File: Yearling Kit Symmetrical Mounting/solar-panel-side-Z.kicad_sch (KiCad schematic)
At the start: 45 parts, among them J1 CON-5040500591, J2 Screw_Terminal_01x02, J3 Screw_Terminal_01x02, J4 Conn_01x01, J5 Conn_01x01, J6 Conn_01x01, J7 Conn_01x01, U1 VEML7700, U2 DRV2605LDGS, U3 MCP9808_DFN, U4 AD8495, U5 ADS1015IDGS, U6 TLVH431 DBZ SOT-23

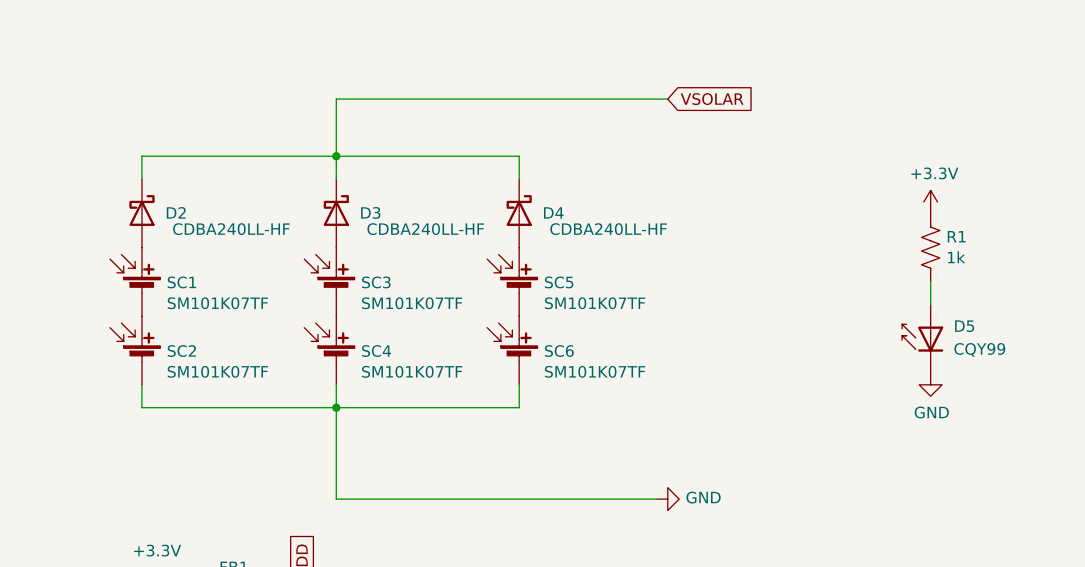
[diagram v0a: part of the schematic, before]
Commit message: -Z Face Mounting Changed
Holes are now symmetrical.
Typos in Silkscreen have been corrected.
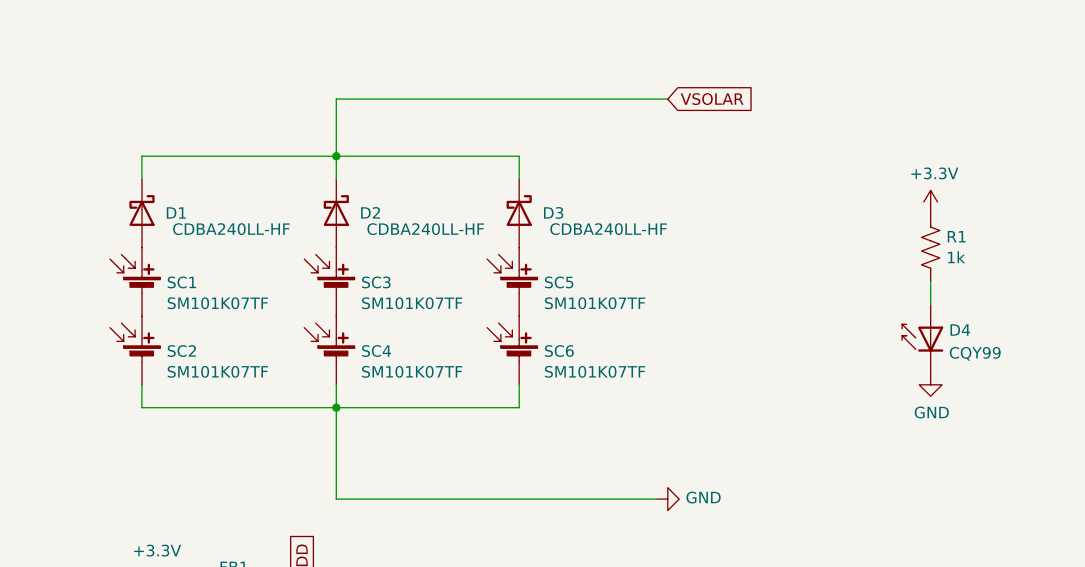
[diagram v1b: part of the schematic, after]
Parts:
- renumbered D2 to D1, D3 to D2, D4 to D3, D5 to D4
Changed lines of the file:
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@@
   (symbol (lib_id "Device:D_Schottky") (at 176.53 95.25 270) (unit 1)
     (in_bom yes) (on_board yes)
-    (property "Reference" "D2" (id 0) (at 180.34 95.25 90))
+    (property "Reference" "D1" (id 0) (at 180.34 95.25 90))
     (property "Value" "CDBA240LL-HF" (id 1) (at 193.04 97.79 90)
       (effects (font (size 1.27 1.27)) (justify right bottom))
@@
   (symbol (lib_id "Device:D_Schottky") (at 198.12 95.25 270) (unit 1)
     (in_bom yes) (on_board yes)
-    (property "Reference" "D3" (id 0) (at 201.93 95.25 90))
+    (property "Reference" "D2" (id 0) (at 201.93 95.25 90))
     (property "Value" "CDBA240LL-HF" (id 1) (at 214.63 97.79 90)
       (effects (font (size 1.27 1.27)) (justify right bottom))
@@
   (symbol (lib_id "Device:D_Schottky") (at 218.44 95.25 270) (unit 1)
     (in_bom yes) (on_board yes)
-    (property "Reference" "D4" (id 0) (at 222.25 95.25 90))
+    (property "Reference" "D3" (id 0) (at 222.25 95.25 90))
     (property "Value" "CDBA240LL-HF" (id 1) (at 234.95 97.79 90)
       (effects (font (size 1.27 1.27)) (justify right bottom))
@@
   (symbol (lib_id "LED:CQY99") (at 264.16 107.95 90) (unit 1)
     (in_bom yes) (on_board yes) (fields_autoplaced)
-    (property "Reference" "D5" (id 0) (at 266.7 107.8229 90)
+    (property "Reference" "D4" (id 0) (at 266.192 108.2583 90)
       (effects (font (size 1.27 1.27)) (justify right))
     )
-    (property "Value" "CQY99" (id 1) (at 266.7 110.3629 90)
+    (property "Value" "CQY99" (id 1) (at 266.192 110.7952 90)
       (effects (font (size 1.27 1.27)) (justify right))
     )
@@
     )
     (path "/00000000-0000-0000-0000-000061067859"
+      (reference "D1") (unit 1) (value "CDBA240LL-HF") (footprint "SolarPanelBoards:DO-214AC")
+    )
+    (path "/00000000-0000-0000-0000-000061455d66"
       (reference "D2") (unit 1) (value "CDBA240LL-HF") (footprint "SolarPanelBoards:DO-214AC")
     )
-    (path "/00000000-0000-0000-0000-000061455d66"
+    (path "/00000000-0000-0000-0000-000062735b03"
       (reference "D3") (unit 1) (value "CDBA240LL-HF") (footprint "SolarPanelBoards:DO-214AC")
     )
-    (path "/00000000-0000-0000-0000-000062735b03"
-      (reference "D4") (unit 1) (value "CDBA240LL-HF") (footprint "SolarPanelBoards:DO-214AC")
-    )
     (path "/ec658cd6-7df5-4acd-be9c-af4ced9448f8"
-      (reference "D5") (unit 1) (value "CQY99") (footprint "LED_SMD:LED_0603_1608Metric")
+      (reference "D4") (unit 1) (value "CQY99") (footprint "LED_SMD:LED_0603_1608Metric")
     )
     (path "/de07df6c-d7a4-404b-8215-db6fcb6ff39f"
